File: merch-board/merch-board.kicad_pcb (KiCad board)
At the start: 2 copper layers, 86 x 54 mm, 83 parts, among them J1 Piano pads, P1 USB_C_Plug, SW1 BOOT, SW2 RST, SW3 OCT_DOWN, SW4 OCT_UP, SW5 TONE_SEL, U1 NCP1117-3.3_SOT223, U2 W25Q128JVS, U3 RP2040, U4 PCM5100A, U5 TPA6211A1DGN, U6 CY8CMBR3116, Y1 ABM8-272-T3

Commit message: Add LCSC part numbers
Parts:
- C17, C21, C24, C32, C33: value 0.1u -> 100n
- R10, R9: footprint Resistor_SMD:R_0402_1005Metric -> Resistor_SMD:R_0603_1608Metric
- SW1: value BOOT -> BOOTSEL
- SW2: value RST -> RESET
- moved C27 2.05 mm to (139.4, 92.6), turned to 90 degrees
- moved R9 0.67 mm to (134.2, 88.4)
- moved R10 0.64 mm to (137.2, 92.8)
- moved C29 0.35 mm to (131.7, 88.6)
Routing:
- net GND: track 102.5 -> 101.4 mm
- net Net-(U5-IN-): track 1.48 -> 2.30 mm
- net Net-(C26-Pad2): track 1.80 -> 2.36 mm

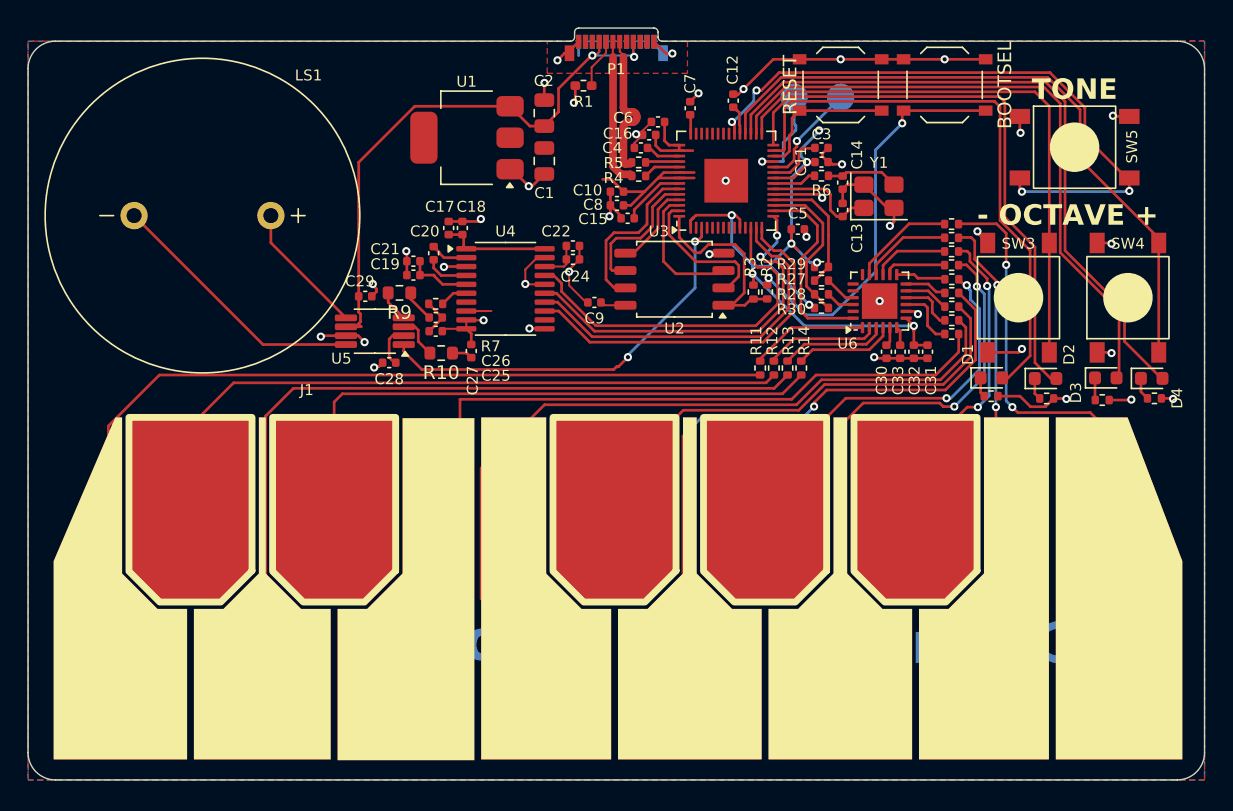
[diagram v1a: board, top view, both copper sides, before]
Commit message: Add volume pot to layout
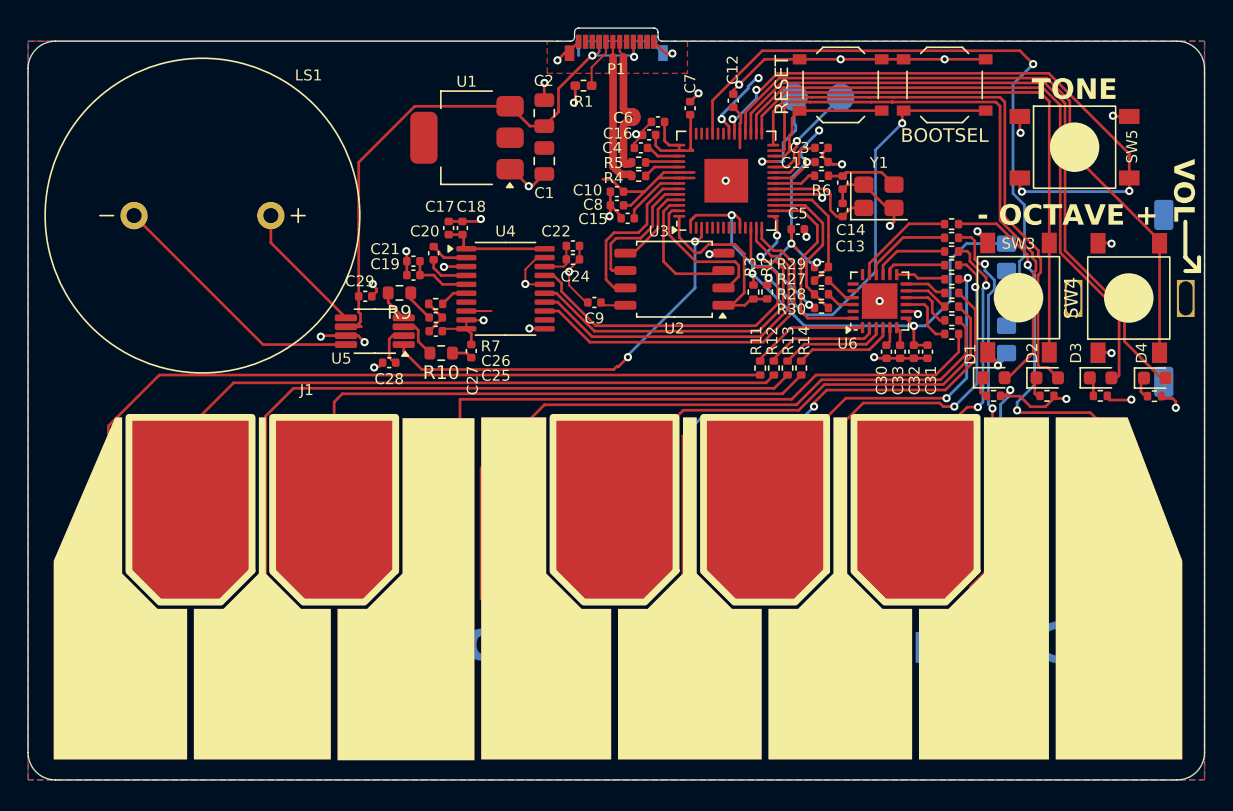
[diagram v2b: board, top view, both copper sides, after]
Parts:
- added RV1: R_Potentiometer, artsfest-touch:Potentiometer_SMD_Alps_RK10J1xR, B.Cu at (187.5, 88.8)
- moved D3 0.38 mm to (185.4, 94.6)
- moved R26 0.34 mm to (185.4, 95.9)
- moved D4 0.23 mm to (189.4, 94.6)
- moved R25 0.19 mm to (181.5, 95.9)
- moved R24 0.18 mm to (177.6, 95.9)
- moved D1 0.18 mm to (177.6, 94.6)
- moved R31 0.16 mm to (189.3, 95.9)
- moved D2 0.13 mm to (181.5, 94.6)
- moved SW4 0.07 mm to (187.5, 88.7)
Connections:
- U3 pad 38: unconnected-(U3-GPIO26_ADC0-Pad38) -> /MCU/POT_VOL
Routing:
- net /MCU/POT_VOL: track 0.00 -> 48.4 mm, vias 0 -> 1
- net +3V3: track 88.0 -> 101.5 mm
- net unconnected-(U3-GPIO23-Pad35): track 0.00 -> 5.49 mm, vias 0 -> 2
- net GND: track 101.4 -> 105.5 mm, vias 40 -> 41
- net Net-(J1-Pin_13): track 44.4 -> 45.4 mm
- net /LED_OCT0: track 41.8 -> 42.3 mm
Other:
- board text added: "VOL"

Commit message: Add artwork
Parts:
- added REF**: LOGO, artsfest-art:Logo-ArtsCluster, B.Cu at (169.1, 112.5)
- added REF**: Building, artsfest-art:Building, B.Cu at (127.3, 105.7)
- added REF**: Logo-Artsfest, artsfest-art:Logo-Artsfest, B.Cu at (181.8, 112.7)
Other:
- board text added: "Design @kaine119"
- board text removed: "Cu cutout"
- board text removed: "Exposed Cu"
- board text removed: "Silkscreen"

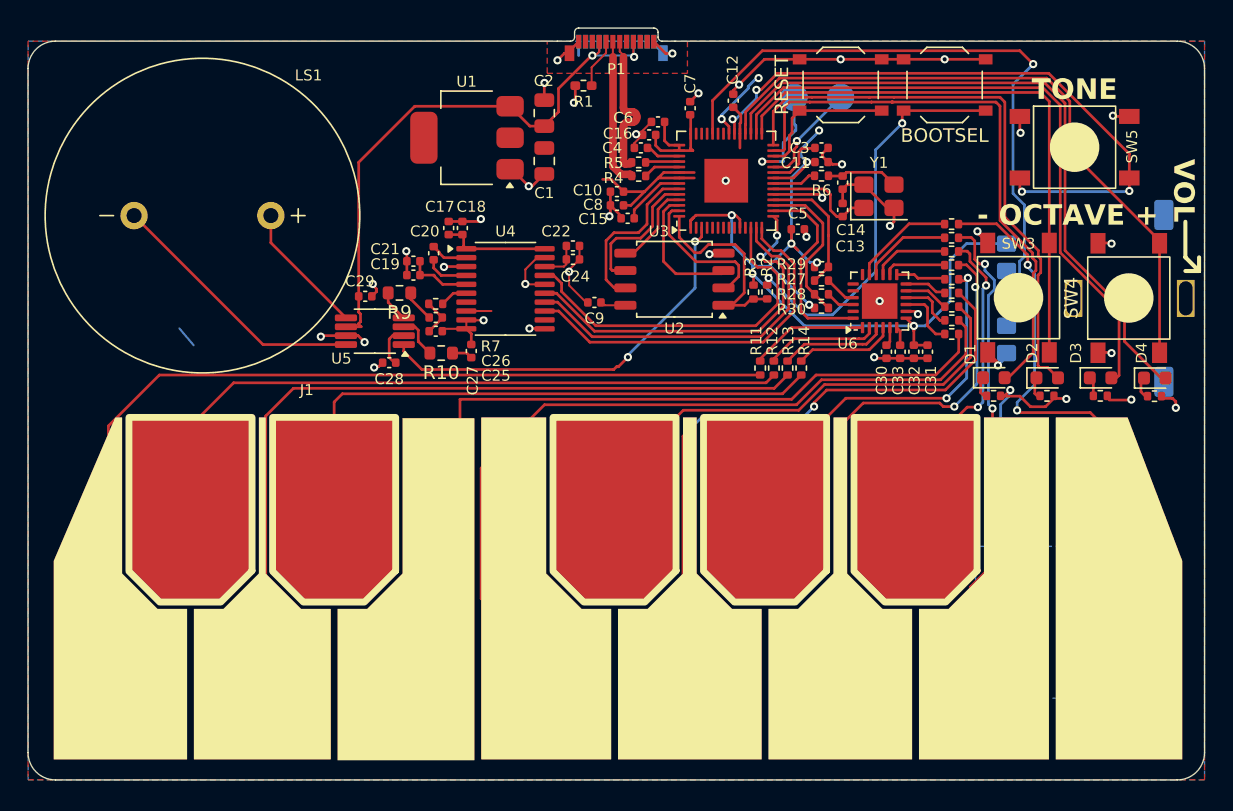
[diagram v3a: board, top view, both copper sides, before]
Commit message: Add WS2812B-2020 for tone indicator
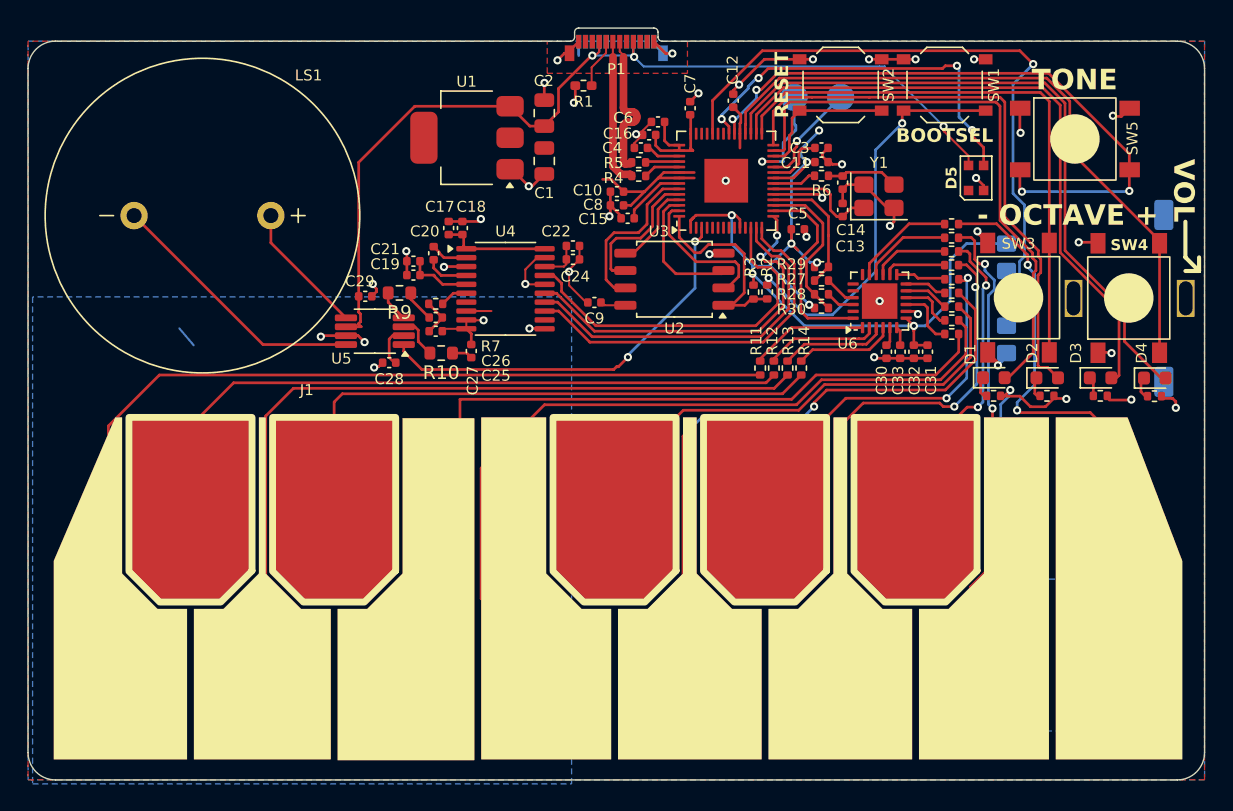
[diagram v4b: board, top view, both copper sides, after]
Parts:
- added D5: WS2812B-2020, LED_SMD:LED_WS2812B-2020_PLCC4_2.0x2.0mm, F.Cu at (176.3, 80.0)
- added G***: LOGO, LOGO, B.Cu at (139.5, 77.0)
- added REF**: OSHW-Logo_5.7x6mm_SilkScreen, Symbol:OSHW-Logo_5.7x6mm_SilkScreen, B.Cu at (183.5, 104.6)
- moved REF** 3.03 mm to (171.0, 114.9)
- moved REF** 2.90 mm to (183.5, 115.1)
- moved SW5 0.60 mm to (183.5, 77.1)
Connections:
- U3 pad 35: unconnected-(U3-GPIO23-Pad35) -> /MCU/LED_TONE_WS2812
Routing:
- net /MCU/LED_TONE_WS2812: track 0.00 -> 28.5 mm, vias 0 -> 4
- net VBUS: track 43.9 -> 72.3 mm, vias 2 -> 3
- net GND: track 105.5 -> 99.6 mm, vias 41 -> 44
- net unconnected-(U3-GPIO23-Pad35): track 5.49 -> 0.00 mm, vias 2 -> 0
- net /MCU/BTN_TONE_SEL: track 46.0 -> 46.6 mm
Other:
- board text added: "Arts Fiesta merch board Prototype R1"
- board text added: "JLCJLCJLCJLC"

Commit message: Add bands logo
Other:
- board text removed: "Arts Fiesta merch board Prototype R1"
